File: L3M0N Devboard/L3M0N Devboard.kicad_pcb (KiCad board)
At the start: 2 copper layers, 21 x 51 mm, 33 parts, among them J1 USB_C_Receptacle_USB2.0_14P, J2 Conn_01x20, J3 Conn_01x20, J4 Conn_01x03, SW1 SW_Push, U1 MCP1700x-330xxTT, U2 RP2040, U3 W25Q128JVS, Y1 12 MHz

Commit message: started some of the wiring
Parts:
- U3: value W25Q128JVS -> W25Q16JVZPIQ TR; footprint Package_SO:SOIC-8_5.3x5.3mm_P1.27mm -> Package_SON:Winbond_USON-8-1EP_3x2mm_P0.5mm_EP0.2x1.6mm
- moved C2 113.3 mm to (133.9, 85.8)
- moved C7 109.2 mm to (133.4, 81.2)
- moved C16 109.1 mm to (131.1, 92.0), turned to 90 degrees
- moved C5 108.3 mm to (134.0, 79.8), turned to 45 degrees
- moved C4 107.7 mm to (132.5, 79.7), turned to 90 degrees
- moved C15 105.8 mm to (125.8, 91.9), turned to 90 degrees
- moved C1 104.8 mm to (122.8, 86.0), turned to 180 degrees
- moved C12 102.5 mm to (131.4, 79.6), turned to 90 degrees
- moved C3 101.3 mm to (123.8, 81.2), turned to 180 degrees
- moved U2 98.9 mm to (128.5, 84.7)
- moved R3 97.7 mm to (130.1, 79.5), turned to -90 degrees
- moved R5 97.7 mm to (128.8, 89.6), turned to 180 degrees
- moved R4 96.4 mm to (129.1, 79.5), turned to -90 degrees
- moved J1 96.0 mm to (128.5, 57.7), turned to 180 degrees
- moved C17 95.2 mm to (125.8, 74.9), turned to 180 degrees
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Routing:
- net USBD+: track 0.00 -> 23.1 mm
- net USBD-: track 0.00 -> 23.0 mm
- net QSPI_SS: track 0.00 -> 7.96 mm
- net QSPI_SD1: track 0.00 -> 7.50 mm
- net QSPI_SD2: track 0.00 -> 5.80 mm
- net QSPI_SD3: track 0.00 -> 5.67 mm
- net QSPI_SCLK: track 0.00 -> 4.95 mm
- net QSPI_SD0: track 0.00 -> 4.01 mm
- net Net-(U2-USB_DP): track 0.00 -> 1.39 mm
- net Net-(U2-USB_DM): track 0.00 -> 1.32 mm

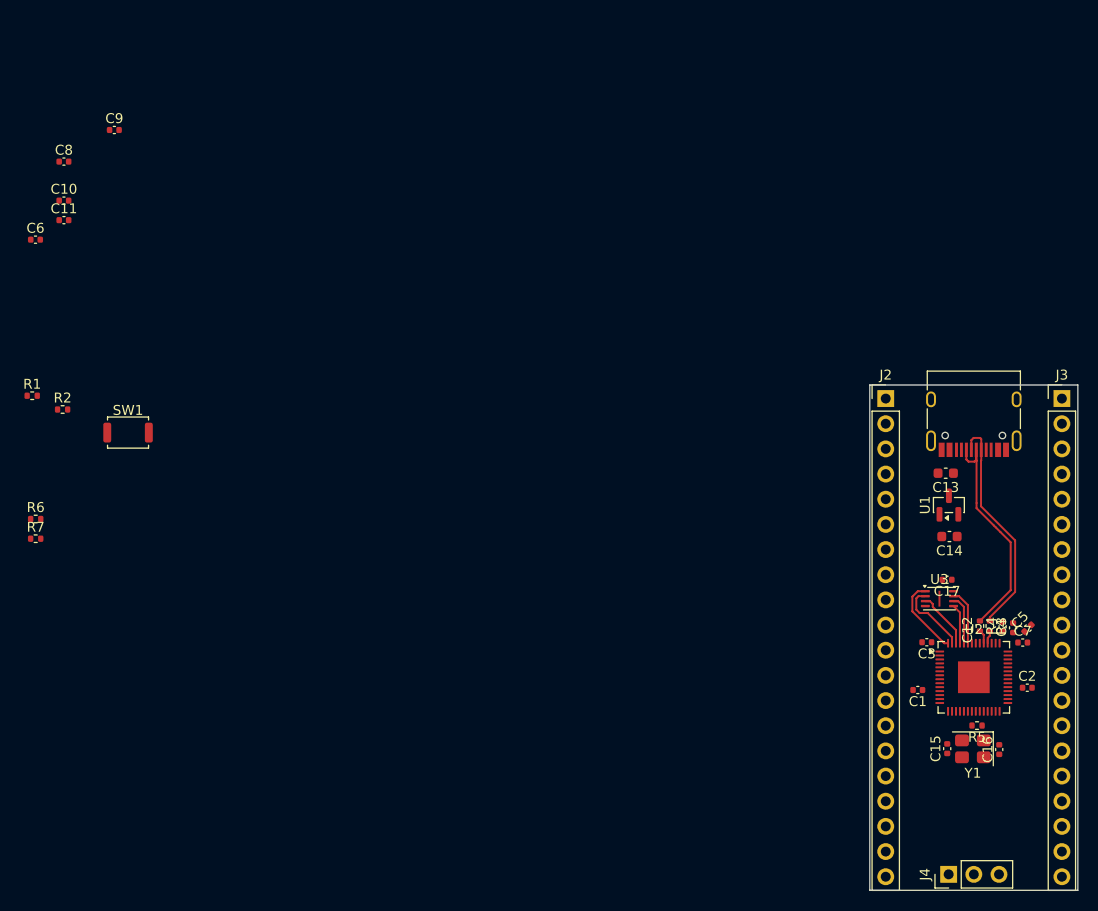
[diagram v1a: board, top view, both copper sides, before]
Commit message: Wired up the left side of the devboard (Besides GND)
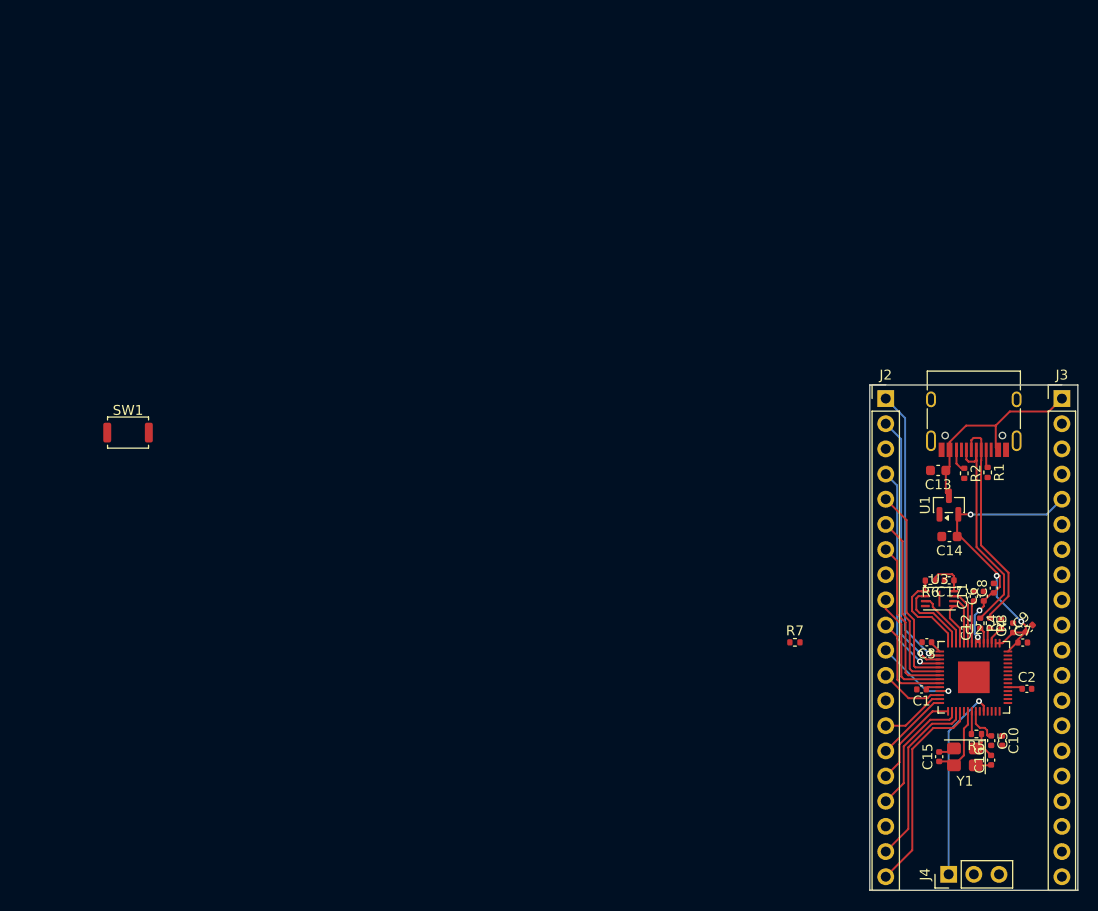
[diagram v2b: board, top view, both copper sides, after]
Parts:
- moved C10 109.3 mm to (131.4, 91.1), turned to -90 degrees
- moved C9 105.1 mm to (134.1, 79.8), turned to 45 degrees
- moved C8 103.3 mm to (130.5, 75.7), turned to 90 degrees
- moved C6 102.2 mm to (129.5, 76.5), turned to 90 degrees
- moved C11 99.4 mm to (128.5, 76.5), turned to 90 degrees
- moved R1 96.7 mm to (129.9, 64.0), turned to -90 degrees
- moved R2 91.2 mm to (127.5, 64.1), turned to -90 degrees
- moved R6 90.5 mm to (124.1, 75.0), turned to 180 degrees
- moved R7 77.3 mm to (110.5, 81.2)
- moved C5 11.9 mm to (130.3, 91.1), turned to -90 degrees
- moved C16 1.35 mm to (130.2, 93.1)
- moved Y1 1.15 mm to (127.6, 92.8)
- moved C15 1.15 mm to (125.0, 92.7)
- moved R5 0.85 mm to (128.8, 90.4)
- moved C13 0.81 mm to (124.9, 63.8)
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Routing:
- net +3V3: track 0.00 -> 53.4 mm, vias 0 -> 5
- net GPIO0: track 0.00 -> 28.7 mm, vias 0 -> 1
- net GPIO1: track 0.00 -> 26.8 mm, vias 0 -> 1
- net GPIO2: track 0.00 -> 22.4 mm, vias 0 -> 1
- net VBUS: track 0.00 -> 21.4 mm
- net GPIO15: track 0.00 -> 21.0 mm
- net GPIO3: track 0.00 -> 20.7 mm
- net SWCLK: track 0.00 -> 20.0 mm, vias 0 -> 1
- net GPIO4: track 0.00 -> 18.7 mm
- net GPIO14: track 0.00 -> 18.3 mm
- net GPIO5: track 0.00 -> 16.8 mm
- net GPIO13: track 0.00 -> 13.0 mm
- net GPIO6: track 0.00 -> 12.4 mm
- net GPIO7: track 0.00 -> 10.4 mm
- net GPIO12: track 0.00 -> 10.1 mm
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
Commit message: added left wires and ground fill
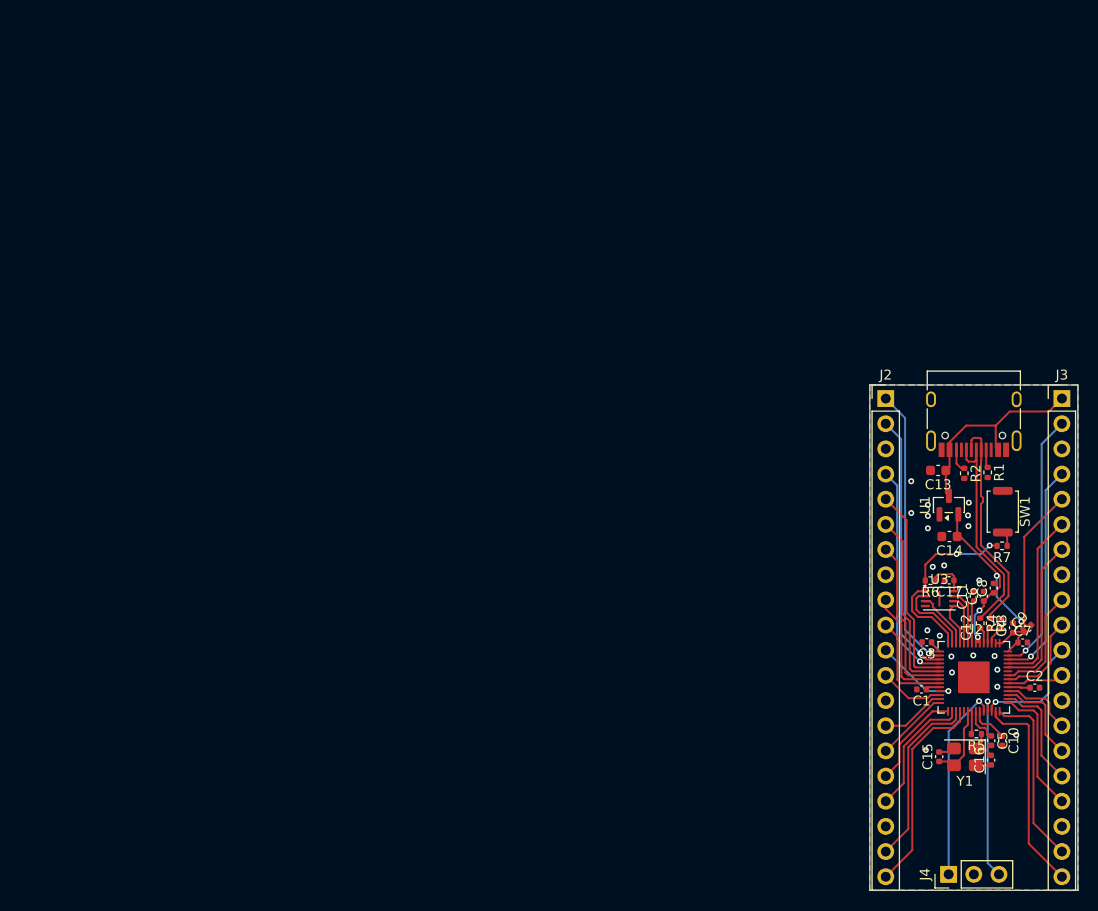
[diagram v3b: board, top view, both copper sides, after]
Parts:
- moved SW1 88.6 mm to (131.4, 68.0), turned to -90 degrees
- moved R7 23.1 mm to (131.4, 71.5), turned to 180 degrees
- moved C2 0.81 mm to (134.7, 85.8)
- moved C9 0.15 mm to (133.9, 79.8)
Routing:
- net GPIO29_ADC3: track 0.00 -> 26.4 mm, vias 0 -> 1
- net GPIO28_ADC2: track 0.00 -> 22.2 mm, vias 0 -> 1
- net GPIO16: track 0.00 -> 20.9 mm
- net SWD: track 0.00 -> 18.9 mm, vias 0 -> 1
- net GPIO17: track 0.00 -> 18.2 mm
- net GPIO27_ADC1: track 0.00 -> 17.7 mm
- net GPIO26_ADC0: track 0.00 -> 15.7 mm
- net GPIO18: track 0.00 -> 13.3 mm
- net RUN: track 0.00 -> 11.7 mm, vias 0 -> 1
- net GPIO19: track 0.00 -> 11.3 mm
- net GPIO24: track 0.00 -> 11.3 mm
- net QSPI_SS: track 9.62 -> 19.3 mm, vias 0 -> 2
- net GPIO20: track 0.00 -> 9.51 mm
- net GPIO23: track 0.00 -> 9.31 mm
- net GPIO21: track 0.00 -> 7.52 mm
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- added copper zone on B.Cu, net (none)
- added copper zone on F.Cu, net (none)

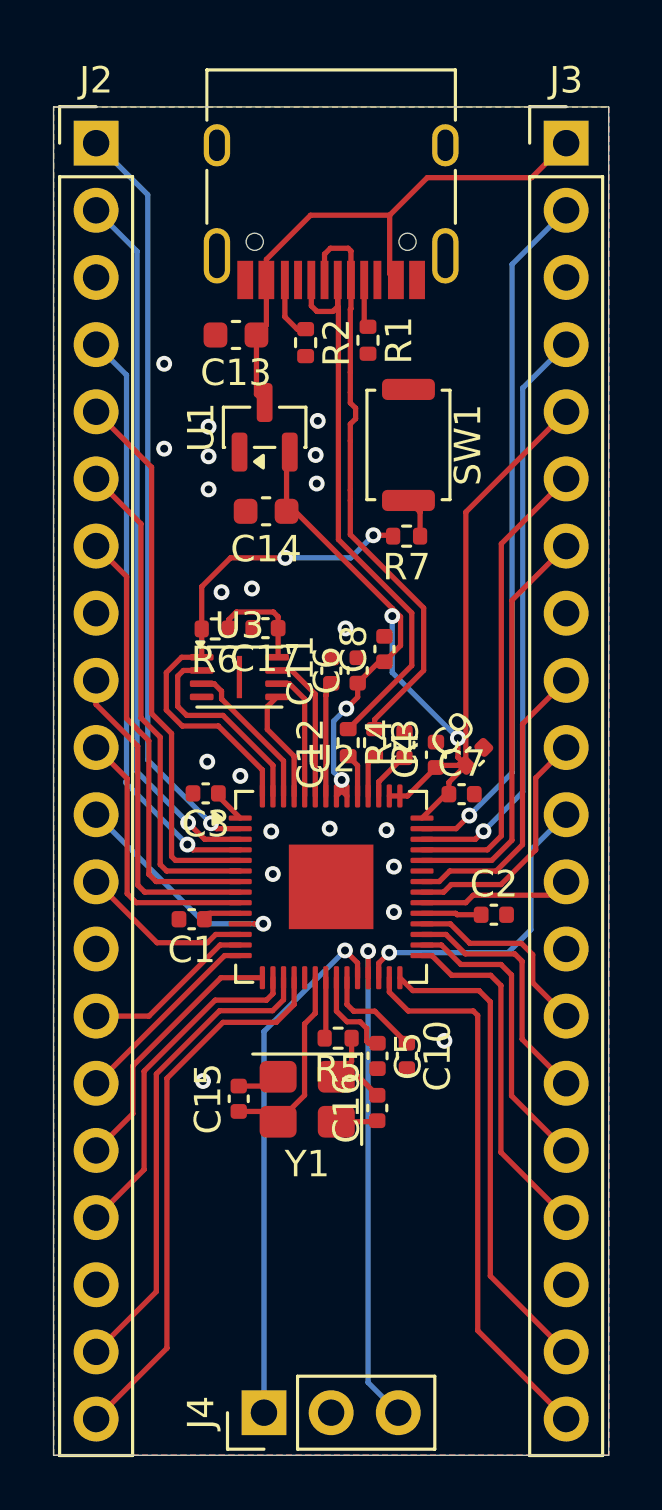
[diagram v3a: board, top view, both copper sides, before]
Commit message: fixed ground fill and silkscreen and added things to silkscreen
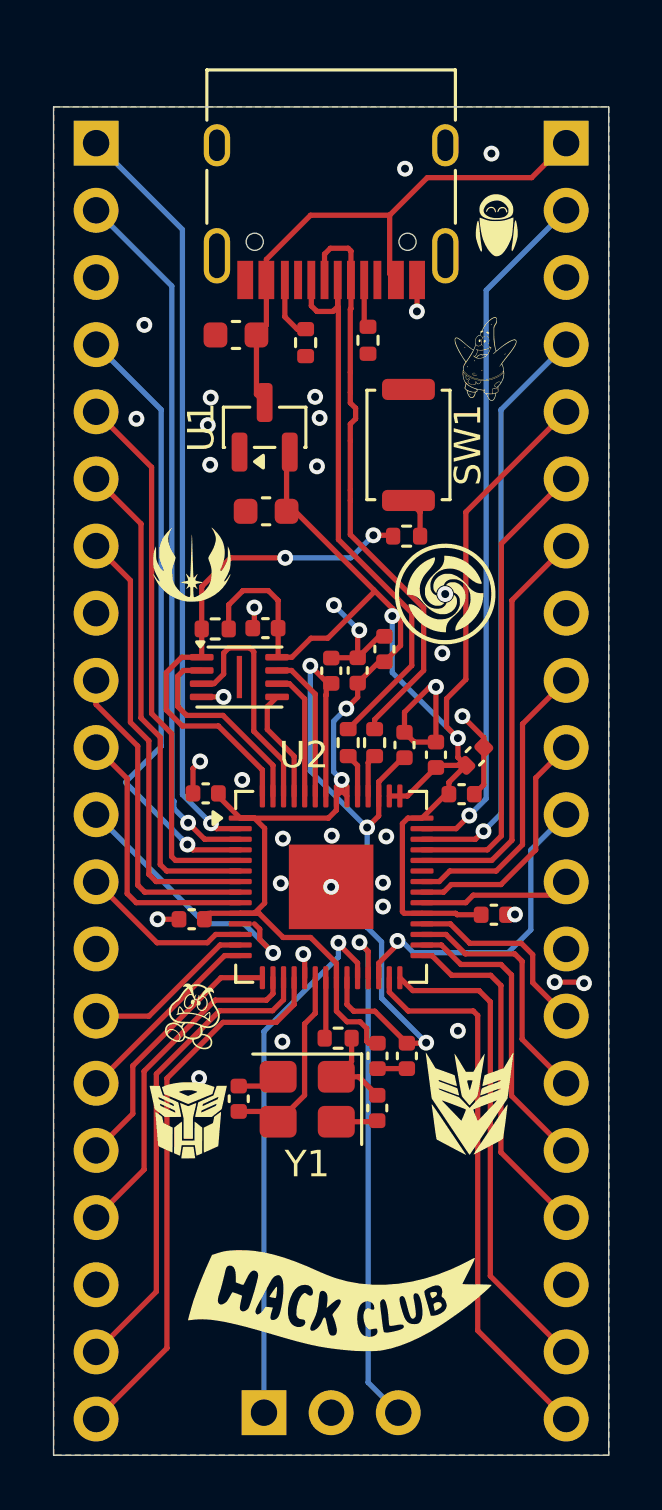
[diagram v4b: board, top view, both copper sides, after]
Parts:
- added G***: LOGO, KiCad-SSD1306-0.91-OLED-4pin-128x32.pretty-master:starwars, F.Cu at (123.2, 72.5)
- added G***: LOGO, KiCad-SSD1306-0.91-OLED-4pin-128x32.pretty-master:lemon, B.Cu at (128.8, 78.6)
- added G***: LOGO, KiCad-SSD1306-0.91-OLED-4pin-128x32.pretty-master:bubbles, B.Cu at (129.0, 95.8)
- added G***: LOGO, KiCad-SSD1306-0.91-OLED-4pin-128x32.pretty-master:jjk, F.Cu at (132.8, 73.6)
- added G***: LOGO, KiCad-SSD1306-0.91-OLED-4pin-128x32.pretty-master:goomba, F.Cu at (123.3, 89.6)
- added G***: LOGO, KiCad-SSD1306-0.91-OLED-4pin-128x32.pretty-master:pstar, F.Cu at (134.3, 64.7)
- added G***: LOGO, KiCad-SSD1306-0.91-OLED-4pin-128x32.pretty-master:hackclub, F.Cu at (128.6, 100.5)
- added G***: LOGO, KiCad-SSD1306-0.91-OLED-4pin-128x32.pretty-master:autobots, F.Cu at (123.1, 93.5)
- added G***: LOGO, KiCad-SSD1306-0.91-OLED-4pin-128x32.pretty-master:decepticon, F.Cu at (133.7, 92.9)
- added G***: LOGO, KiCad-SSD1306-0.91-OLED-4pin-128x32.pretty-master:eva, F.Cu at (134.8, 59.7)
- added G***: LOGO, KiCad-SSD1306-0.91-OLED-4pin-128x32.pretty-master:zane, B.Cu at (128.9, 64.2)
- J2, J3, J4: moved to B.Cu
- turned J2 to 180 degrees
- turned J3 to 180 degrees
- turned J4 to -90 degrees
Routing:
- net +3V3: track 57.9 -> 82.6 mm
- net GND: track 3.20 -> 26.5 mm, vias 0 -> 35
- net +1V1: track 10.1 -> 29.4 mm, vias 0 -> 3
- net QSPI_SD2: track 5.80 -> 8.97 mm
- net GPIO8: track 8.37 -> 10.3 mm
- net GPIO2: track 22.4 -> 23.5 mm
- net SWD: track 18.9 -> 19.9 mm
- net SWCLK: track 20.0 -> 20.6 mm
- net (no net): vias 21 -> 1
- added copper zone on B.Cu, net GND
- added copper zone on F.Cu, net GND
- removed copper zone on B.Cu, net (none)
- removed copper zone on F.Cu, net (none)

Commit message: made the gerber file
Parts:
- added G***: LOGO, KiCad-SSD1306-0.91-OLED-4pin-128x32.pretty-master:httyd, F.Cu at (130.9, 97.0)
- added G***: LOGO, KiCad-SSD1306-0.91-OLED-4pin-128x32.pretty-master:toot, F.Cu at (125.1, 96.9)
- moved G*** 0.65 mm to (128.7, 101.2)

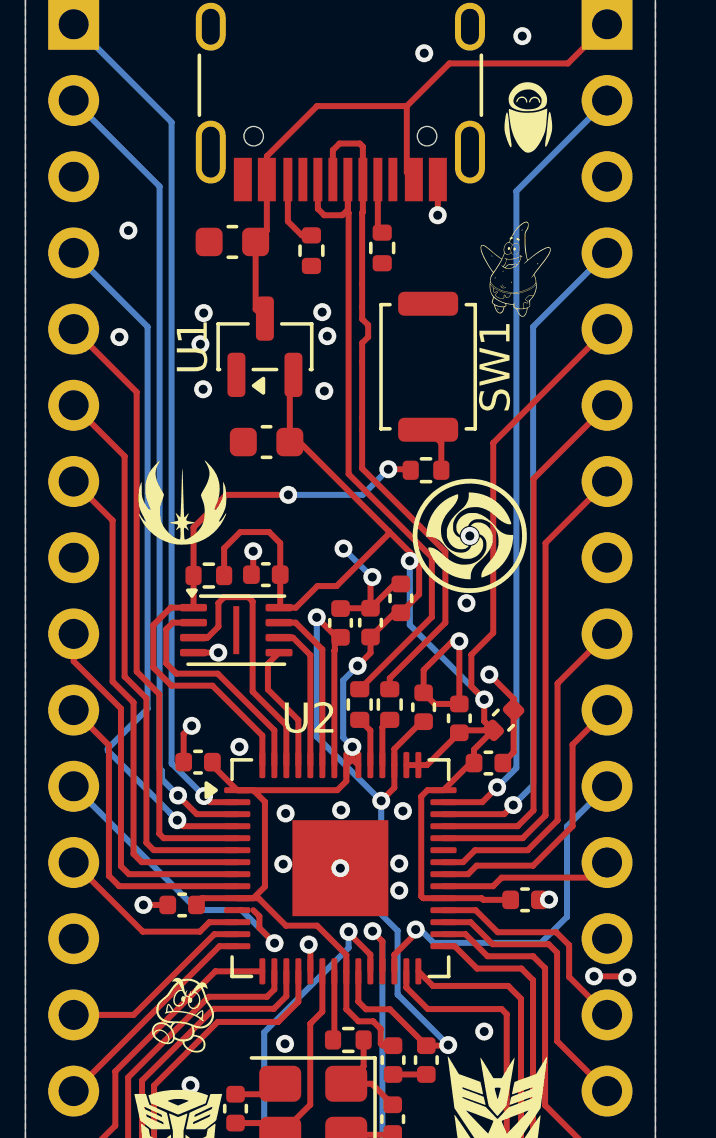
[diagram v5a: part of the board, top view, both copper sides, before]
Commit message: Added LED and updated ReadMe
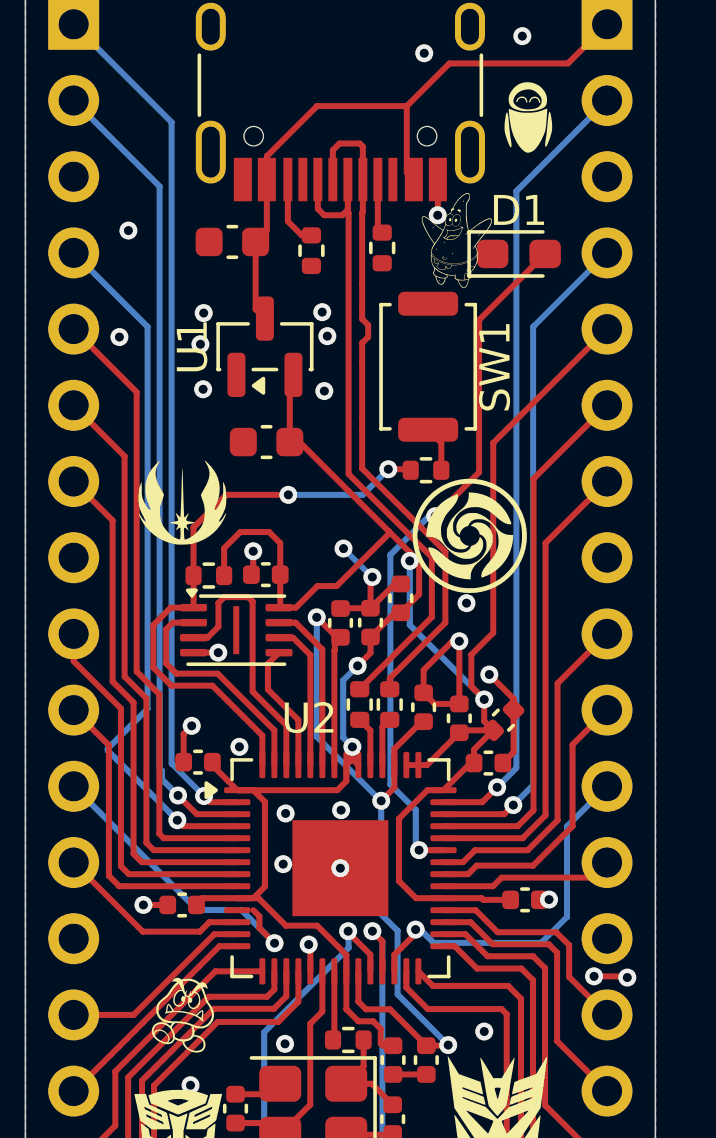
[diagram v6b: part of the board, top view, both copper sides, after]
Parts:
- added D1: LED, LED_SMD:LED_0603_1608Metric_Pad1.05x0.95mm_HandSolder, F.Cu at (134.5, 64.2)
- moved G*** 2.18 mm to (132.4, 63.8)
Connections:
- U2 pad 37: unconnected-(U2-GPIO25-Pad37) -> GPIO25
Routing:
- net GPIO25: track 0.00 -> 23.3 mm, vias 0 -> 2
- net +3V3: track 82.6 -> 83.4 mm
- net GND: vias 35 -> 32
- net (no net): vias 1 -> 0
